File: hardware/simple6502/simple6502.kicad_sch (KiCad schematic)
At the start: 20 parts, among them J1 ~{VP}, J2 CLK SEL, J3 RESET, J4 6502 BUS, SW1 RESET, T1 DS1813-10+, U1 W65C02SxP, U2 CY62256-70PC, U3 28C256, U4 74LS30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

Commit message: PCB defaults set and components dropped
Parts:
- removed J4: 6502 BUS, Connector_Card:EDAC 395-050-520-201, symbol Connector_Generic:Conn_02x25_Counter_Clockwise
- U1: footprint Package_DIP:DIP-40_W15.24mm -> Package_DIP:DIP-40_W15.24mm_Socket
- U2: footprint Package_DIP:DIP-28_W15.24mm -> Package_DIP:DIP-28_W15.24mm_Socket
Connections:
- net ~{VP}: now reaches J1.2 (Pin_2), U1.1 (~{VP})
- no-connect marks 15 -> 3
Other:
- note removed: "BUS Connector: EDAC 395-050-520-201"

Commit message: First PCB Layout
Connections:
- net VCC: now also R3.2; no longer R3.1
- net BE: now reaches R4.1, U1.36 (BE)
- net RDY: now reaches U1.2 (RDY)
- net RDY: now also R3.1; no longer R3.2
- net ~{SO}: now reaches R5.1, U1.38 (~{SO})
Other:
- moved on the sheet: R3
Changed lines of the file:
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@@
+    (effects (font (size 1.27 1.27)) (justify left bottom))
+  )
+  (label "~{SO}" (at 45.72 74.93 0) (fields_autoplaced)
     (effects (font (size 1.27 1.27)) (justify left bottom))
   )
@@
     (effects (font (size 1.27 1.27)) (justify right bottom))
   )
+  (label "BE" (at 45.72 59.69 0) (fields_autoplaced)
+    (effects (font (size 1.27 1.27)) (justify left bottom))
+  )
   (label "D5" (at 232.41 44.45 0) (fields_autoplaced)
     (effects (font (size 1.27 1.27)) (justify left bottom))
@@
   (label "A2" (at 128.27 36.83 180) (fields_autoplaced)
     (effects (font (size 1.27 1.27)) (justify right bottom))
+  )
+  (label "RDY" (at 45.72 57.15 0) (fields_autoplaced)
+    (effects (font (size 1.27 1.27)) (justify left bottom))
   )
   (label "A14" (at 128.27 67.31 180) (fields_autoplaced)
@@
     )
   )
-  (symbol (lib_name "R_1") (lib_id "Device:R") (at 33.02 57.15 90) (unit 1)
+  (symbol (lib_name "R_1") (lib_id "Device:R") (at 33.02 57.15 270) (unit 1)
     (in_bom yes) (on_board yes) (dnp no)
-    (property "Reference" "R3" (at 33.02 54.61 90)
+    (property "Reference" "R3" (at 33.02 59.69 90)
       (effects (font (size 1.27 1.27)))
     )
@@
       (effects (font (size 1.27 1.27)))
     )
-    (property "Footprint" "Resistor_THT:R_Axial_DIN0204_L3.6mm_D1.6mm_P7.62mm_Horizontal" (at 33.02 58.928 90)
-      (effects (font (size 1.27 1.27)) hide)
-    )
+    (property "Footprint" "Resistor_THT:R_Axial_DIN0204_L3.6mm_D1.6mm_P7.62mm_Horizontal" (at 33.02 55.372 90)
+      (effects (font (size 1.27 1.27)) hide)
+    )

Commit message: PCB fully routed clean DRC
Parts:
- TP2: footprint TestPoint:TestPoint_THTPad_3.0x3.0mm_Drill1.5mm -> TestPoint:TestPoint_THTPad_2.0x2.0mm_Drill1.0mm
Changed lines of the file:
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@@
       (effects (font (size 1.27 1.27)))
     )
-    (property "Footprint" "TestPoint:TestPoint_THTPad_3.0x3.0mm_Drill1.5mm" (at 204.47 168.91 0)
+    (property "Footprint" "TestPoint:TestPoint_THTPad_2.0x2.0mm_Drill1.0mm" (at 204.47 168.91 0)
       (effects (font (size 1.27 1.27)) hide)
     )

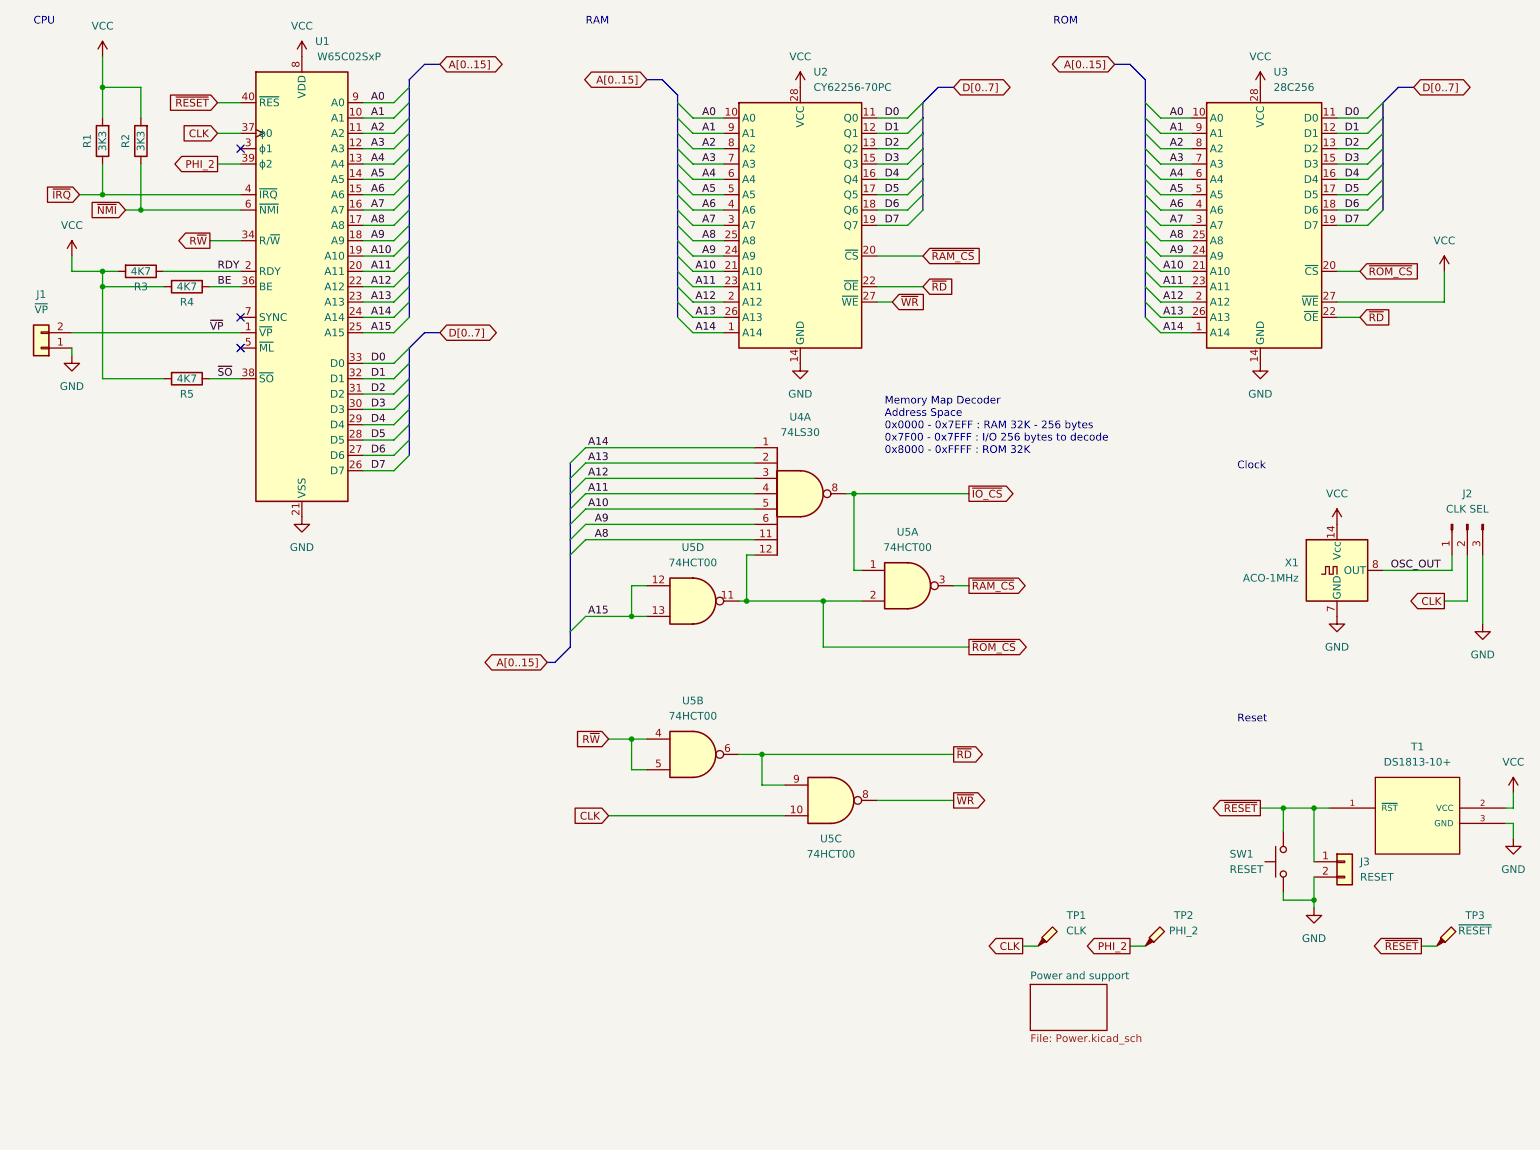
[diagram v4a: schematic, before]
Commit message: added IO 3-8 decoder
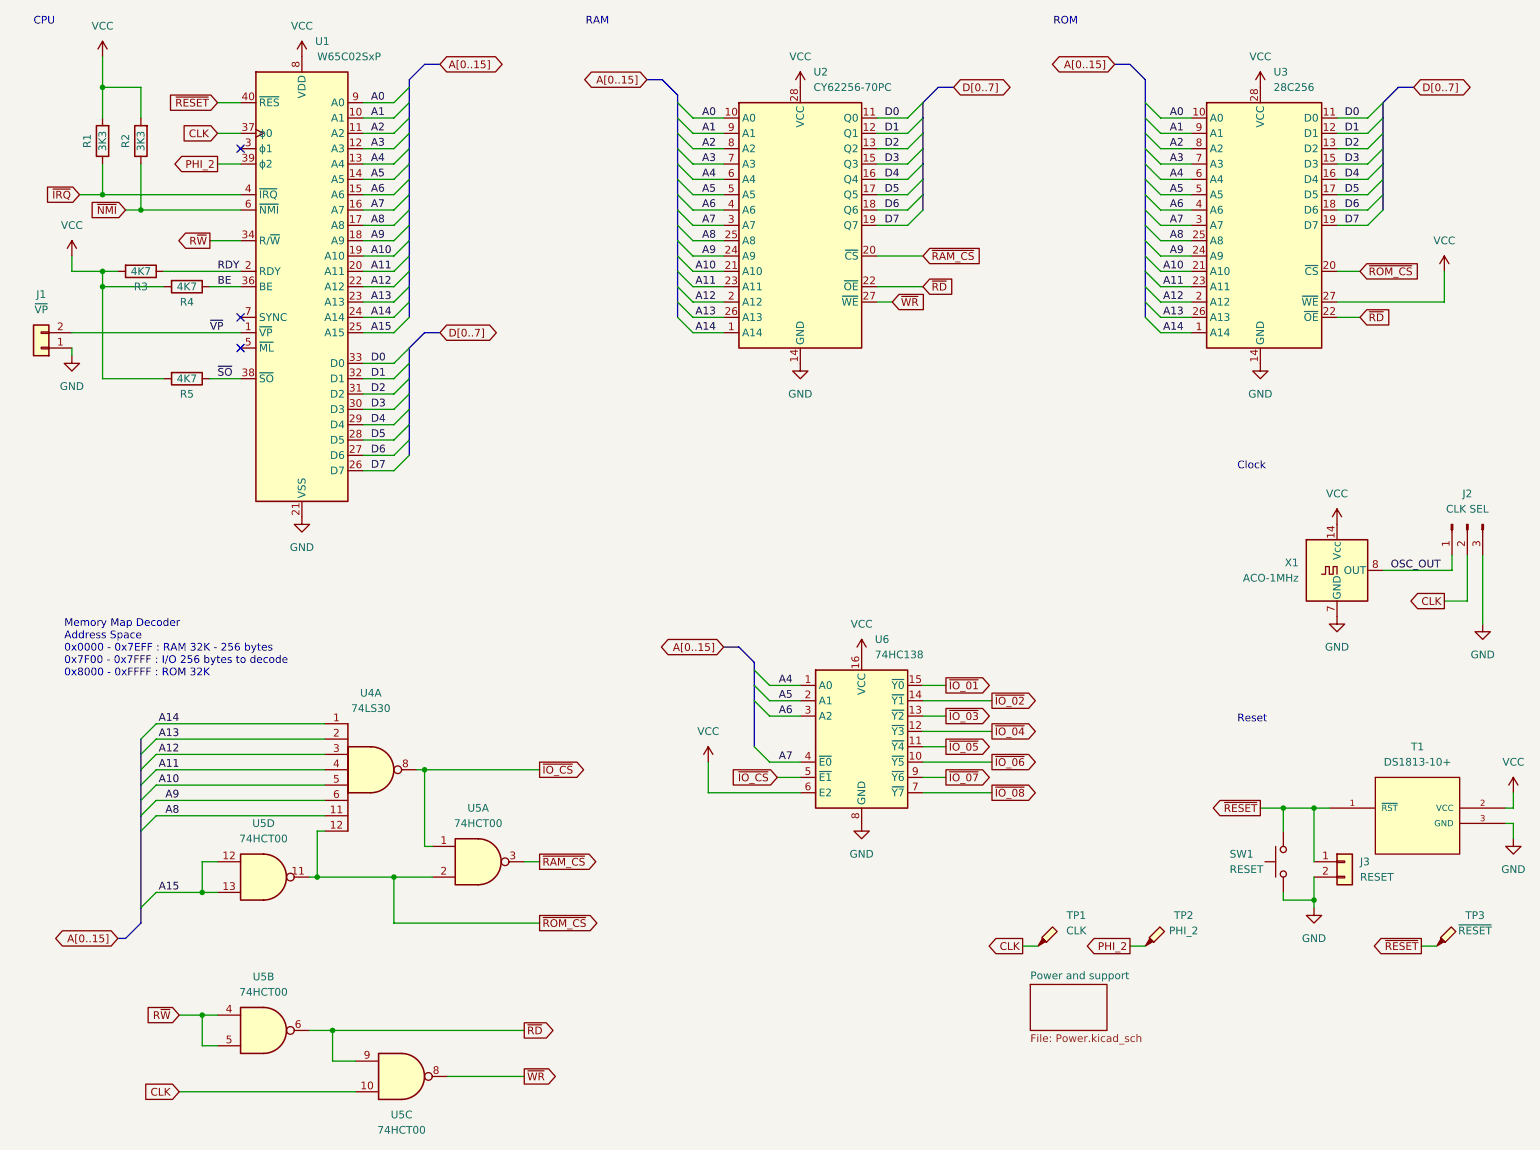
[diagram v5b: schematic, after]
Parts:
- added U6: 74HC138, symbol 74xx:74HC138
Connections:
- net A4: now also U6.1 (A0)
- net A5: now also U6.2 (A1)
- net A6: now also U6.3 (A2)
- net A7: now also U6.4 (~{E0})
- net GND: now also U6.8 (GND)
- net VCC: now also U6.16 (VCC), U6.6 (E2)
- net ~{IO_CS}: now also U6.5 (~{E1})
- new net ~{IO_01}: U6.15 (~{Y0})
- new net ~{IO_02}: U6.14 (~{Y1})
- new net ~{IO_03}: U6.13 (~{Y2})
- new net ~{IO_04}: U6.12 (~{Y3})
- new net ~{IO_05}: U6.11 (~{Y4})
- new net ~{IO_06}: U6.10 (~{Y5})
- new net ~{IO_07}: U6.9 (~{Y6})
- new net ~{IO_08}: U6.7 (~{Y7})
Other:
- moved on the sheet: U4A, U5A, U5B, U5C, U5D

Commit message: more pin rearrangment in bus connector
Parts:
- U2: value CY62256-70PC -> RAM 62256
- U3: value 28C256 -> ROM 28C256
- U6: footprint (none) -> Package_DIP:DIP-16_W7.62mm_Socket
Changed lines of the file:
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@@
       (effects (font (size 1.27 1.27)) (justify left))
     )
-    (property "Value" "CY62256-70PC" (at 144.4341 26.67 0)
+    (property "Value" "RAM 62256" (at 144.4341 26.67 0)
       (effects (font (size 1.27 1.27)) (justify left))
     )
@@
       (effects (font (size 1.27 1.27)) (justify left))
     )
-    (property "Value" "28C256" (at 220.6341 26.67 0)
+    (property "Value" "ROM 28C256" (at 220.6341 26.67 0)
       (effects (font (size 1.27 1.27)) (justify left))
     )
@@
       (effects (font (size 1.27 1.27)) (justify left))
     )
-    (property "Footprint" "" (at 152.4 135.89 0)
-      (effects (font (size 1.27 1.27)) hide)
-    )
+    (property "Footprint" "Package_DIP:DIP-16_W7.62mm_Socket" (at 152.4 135.89 0)
+      (effects (font (size 1.27 1.27)) hide)
+    )

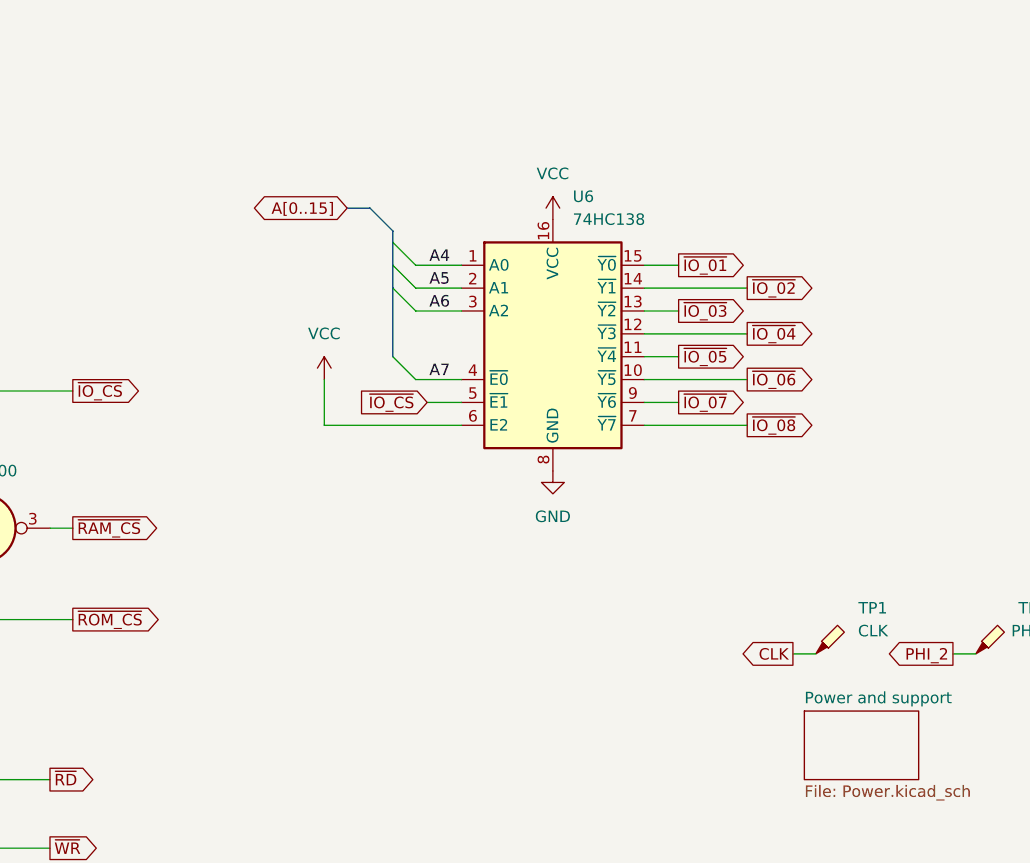
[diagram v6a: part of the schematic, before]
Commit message: Schematics updated to v1 - ERC passed
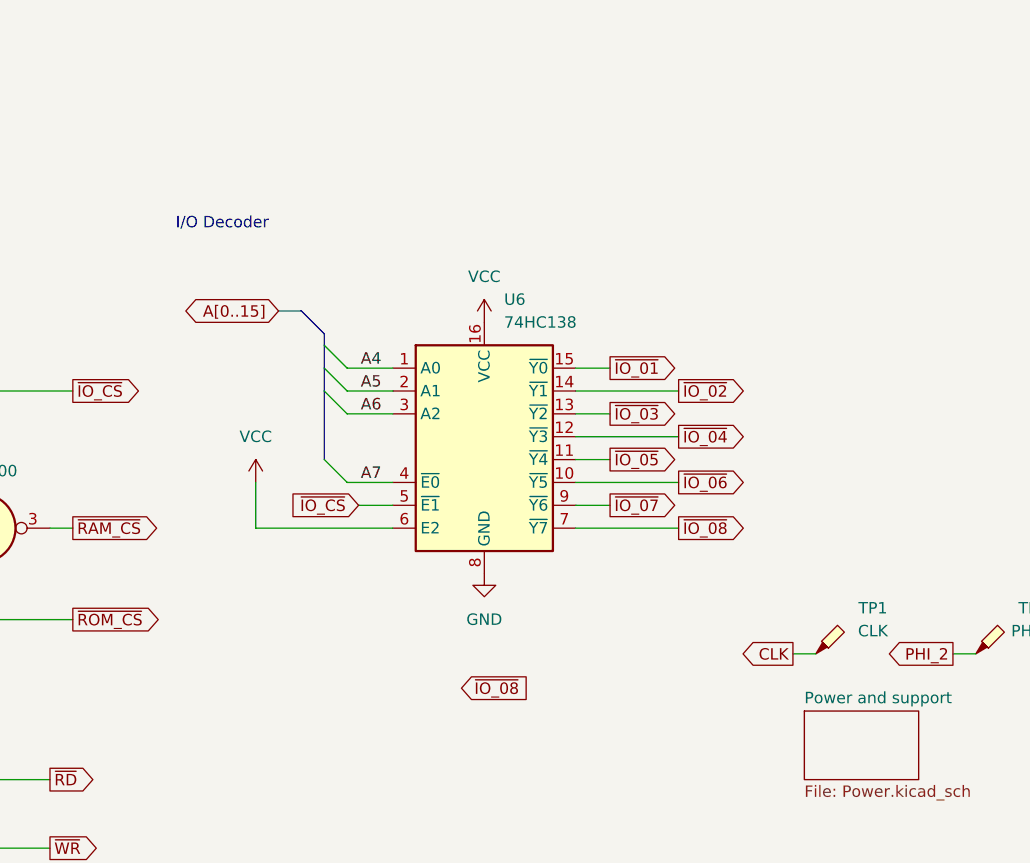
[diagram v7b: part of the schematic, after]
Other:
- note added: "I/O Decoder"
- moved on the sheet: U6

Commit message: Relocated reset
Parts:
- TP1: footprint TestPoint:TestPoint_THTPad_3.0x3.0mm_Drill1.5mm -> TestPoint:TestPoint_THTPad_2.0x2.0mm_Drill1.0mm
- TP2: footprint TestPoint:TestPoint_THTPad_2.0x2.0mm_Drill1.0mm -> TestPoint:TestPoint_THTPad_1.0x1.0mm_Drill0.5mm
- TP3: footprint TestPoint:TestPoint_THTPad_3.0x3.0mm_Drill1.5mm -> TestPoint:TestPoint_THTPad_1.5x1.5mm_Drill0.7mm
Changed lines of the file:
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@@
       (effects (font (size 1.27 1.27)))
     )
-    (property "Footprint" "TestPoint:TestPoint_THTPad_3.0x3.0mm_Drill1.5mm" (at 252.73 168.91 0)
+    (property "Footprint" "TestPoint:TestPoint_THTPad_1.5x1.5mm_Drill0.7mm" (at 252.73 168.91 0)
       (effects (font (size 1.27 1.27)) hide)
     )
@@
       (effects (font (size 1.27 1.27)))
     )
-    (property "Footprint" "TestPoint:TestPoint_THTPad_2.0x2.0mm_Drill1.0mm" (at 204.47 168.91 0)
+    (property "Footprint" "TestPoint:TestPoint_THTPad_1.0x1.0mm_Drill0.5mm" (at 204.47 168.91 0)
       (effects (font (size 1.27 1.27)) hide)
     )
@@
       (effects (font (size 1.27 1.27)))
     )
-    (property "Footprint" "TestPoint:TestPoint_THTPad_3.0x3.0mm_Drill1.5mm" (at 186.69 168.91 0)
-      (effects (font (size 1.27 1.27)) hide)
-    )
+    (property "Footprint" "TestPoint:TestPoint_THTPad_2.0x2.0mm_Drill1.0mm" (at 186.69 168.91 0)
+      (effects (font (size 1.27 1.27)) hide)
+    )
